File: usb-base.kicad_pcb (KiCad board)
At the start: 4 copper layers, 100 x 100 mm, 13 parts, among them J1 USB3_B, U1 CYUSB3082-FCAXI, U2 TPS25221, U3 TPS62161DSG, U4 LFE5U-25F-6BG256C, U6 TPS62162DSG

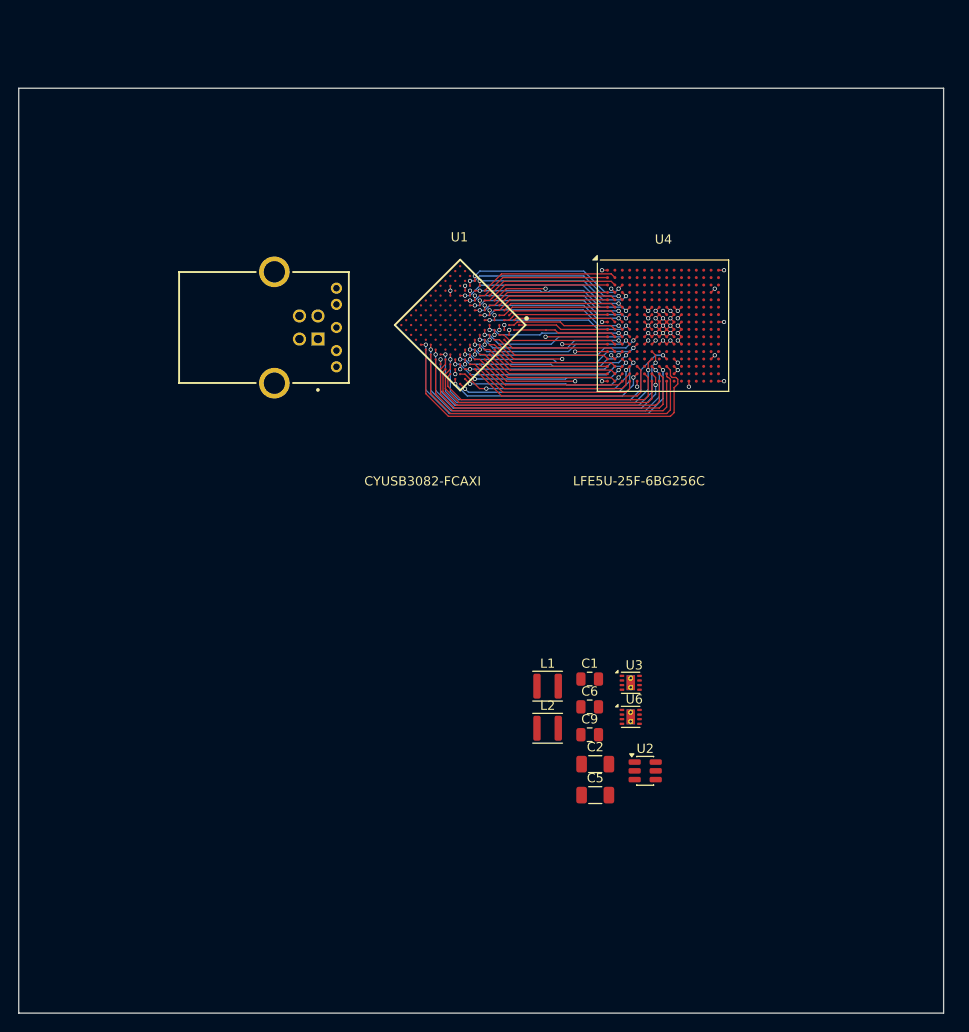
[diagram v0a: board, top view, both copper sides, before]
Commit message: Power supplies, oscillators, user IO breakout
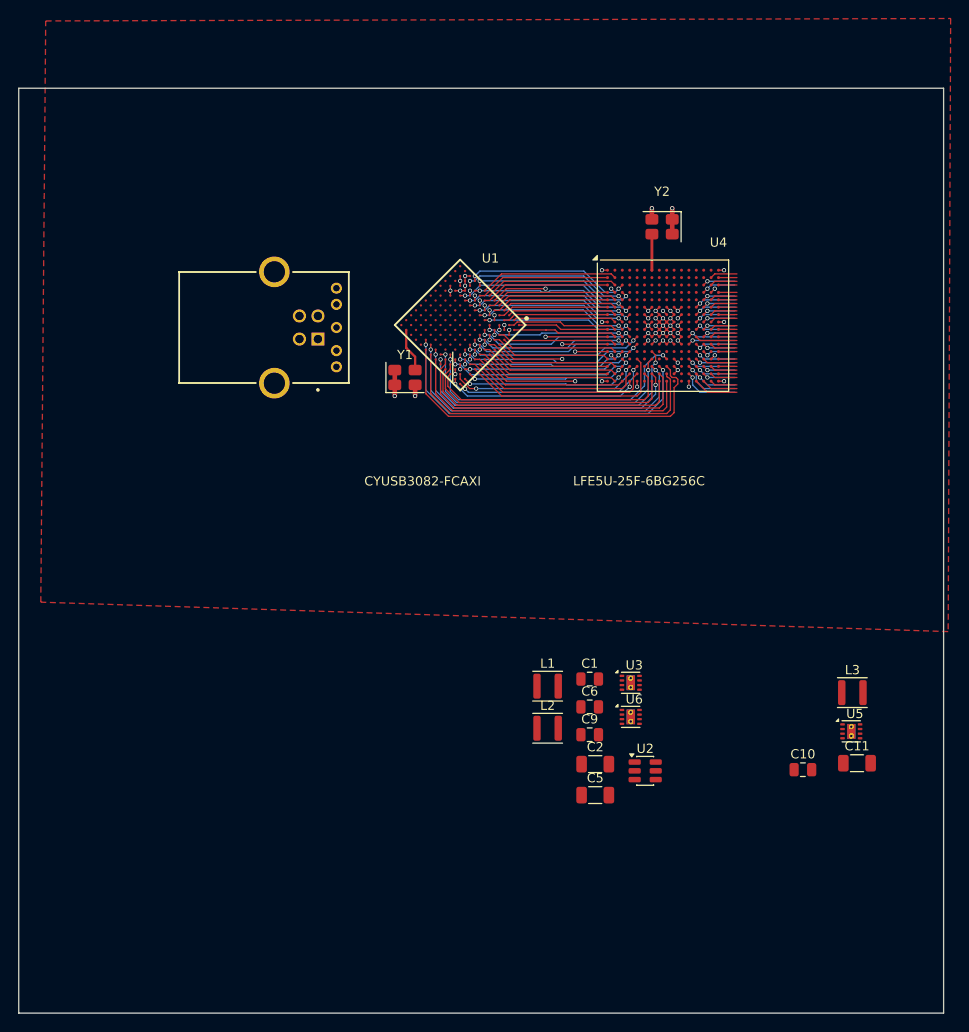
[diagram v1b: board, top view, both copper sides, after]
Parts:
- added C10: 10u, Capacitor_SMD:C_0805_2012Metric, F.Cu at (159.8, 107.2)
- added C11: 22u, Capacitor_SMD:C_1206_3216Metric, F.Cu at (165.7, 106.5)
- added L3: 2.2u, Inductor_SMD:L_Sunlord_SWPA3015S, F.Cu at (165.2, 98.9)
- added U5: TPS62160DSG, Package_SON:WSON-8-1EP_2x2mm_P0.5mm_EP0.9x1.6mm_ThermalVias, F.Cu at (165.1, 103.1)
- added Y1: 24MHz, Crystal:Crystal_SMD_SeikoEpson_TSX3225-4Pin_3.2x2.5mm, F.Cu at (116.8, 64.8)
- added Y2: 25MHz, Crystal:Crystal_SMD_SeikoEpson_TSX3225-4Pin_3.2x2.5mm, F.Cu at (144.6, 48.5)
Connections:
- U1 pad C11: +1V8 -> +3V3
- U1 pad F11: unconnected-(U1C-P13_0_PMODE-PadF11) -> PMODE
- U1 pad J12: unconnected-(U1C-P9_7_I2S0-RXMCLK-PadJ12) -> GPIO_1
- U1 pad J13: GPIO_1 -> unconnected-(U1C-P1_1_CC2-PadJ13)
- U1 pad M12: +1V8 -> +3V3
- U1 pad M13: unconnected-(U1C-P5_1_XTALOUT-PadM13) -> 24MHz
- U4 pad A7: unconnected-(U4B-PT38A/+/PCLKT0_0-PadA7) -> 25MHz
- U4 pad B15: unconnected-(U4D-PR11B/-/URC_GPLL0C_IN/HS/RDQ17-PadB15) -> D0_1
- U4 pad B16: unconnected-(U4D-PR11A/+/URC_GPLL0T_IN/HS/RDQ17-PadB16) -> D0_0
- U4 pad C14: unconnected-(U4D-PR11C/+/RDQ17-PadC14) -> D0_2
- U4 pad C15: unconnected-(U4D-PR14B/-/HS/RDQ17-PadC15) -> D0_5
- U4 pad C16: unconnected-(U4D-PR14A/+/HS/RDQ17-PadC16) -> D0_4
- U4 pad D14: unconnected-(U4D-PR11D/-/RDQ17-PadD14) -> D0_3
- U4 pad D16: unconnected-(U4D-PR17A/+/HS/RDQS17-PadD16) -> D0_8
- U4 pad E14: unconnected-(U4D-PR14C/+/RDQ17-PadE14) -> D0_6
- U4 pad E15: unconnected-(U4D-PR17B/-/HS/RDQSN17-PadE15) -> D0_9
- U4 pad E16: unconnected-(U4D-PR20D/-/RDQ17-PadE16) -> D0_13
- U4 pad F13: unconnected-(U4D-PR17C/+/RDQ17-PadF13) -> D0_10
- U4 pad F14: unconnected-(U4D-PR14D/-/RDQ17-PadF14) -> D0_7
- U4 pad F15: unconnected-(U4D-PR20C/+/RDQ17-PadF15) -> D0_12
- U4 pad F16: unconnected-(U4D-PR23A/+/HS/RDQ29-PadF16) -> D0_14
- U4 pad G13: unconnected-(U4D-PR20B/-/HS/RDQ17-PadG13) -> D0_11
- U4 pad G14: unconnected-(U4D-PR23C/+/VREF1_2/RDQ29-PadG14) -> D0_16
- U4 pad G15: unconnected-(U4D-PR23B/-/HS/RDQ29-PadG15) -> D0_15
- U4 pad G16: unconnected-(U4D-PR29A/+/GR_PCLK2_1/HS/RDQS29-PadG16) -> D0_20
- U4 pad H13: unconnected-(U4D-PR26B/-/HS/RDQ29-PadH13) -> D0_18
- U4 pad H14: unconnected-(U4D-PR23D/-/RDQ29-PadH14) -> D0_17
- U4 pad H15: unconnected-(U4D-PR29B/-/HS/RDQSN29-PadH15) -> D0_21
- U4 pad J13: unconnected-(U4D-PR26C/+/RDQ29-PadJ13) -> D0_19
- U4 pad J14: unconnected-(U4D-PR29C/+/GR_PCLK2_0/RDQ29-PadJ14) -> D0_22
- U4 pad J15: unconnected-(U4D-PR32B/-/PCLKC2_1/HS/RDQ29-PadJ15) -> D0_25
- U4 pad J16: unconnected-(U4D-PR32A/+/PCLKT2_1/HS/RDQ29-PadJ16) -> D0_24
- U4 pad K12: unconnected-(U4E-PR38B/-/HS/RDQ41-PadK12) -> D1_5
- U4 pad K13: unconnected-(U4E-PR38A/+/GR_PCLK3_0/HS/RDQ41-PadK13) -> D1_4
- U4 pad K14: unconnected-(U4D-PR29D/-/RDQ29-PadK14) -> D0_23
- U4 pad K15: unconnected-(U4D-PR32D/-/PCLKC2_0/RDQ29-PadK15) -> D0_27
- U4 pad K16: unconnected-(U4D-PR32C/+/PCLKT2_0/RDQ29-PadK16) -> D0_26
- U4 pad L12: unconnected-(U4E-PR38D/-/RDQ41-PadL12) -> D1_7
- U4 pad L13: unconnected-(U4E-PR38C/+/GR_PCLK3_1/RDQ41-PadL13) -> D1_6
- U4 pad L14: unconnected-(U4E-PR41C/+/RDQ41-PadL14) -> D1_10
- U4 pad L15: unconnected-(U4E-PR35B/-/PCLKC3_1/HS/RDQ41-PadL15) -> D1_1
- U4 pad L16: unconnected-(U4E-PR35A/+/PCLKT3_1/HS/RDQ41-PadL16) -> D1_0
- U4 pad M12: unconnected-(U4E-PR65C/+/RDQ65-PadM12) -> D1_25
- U4 pad M13: unconnected-(U4E-PR44C/+/RDQ41-PadM13) -> D1_14
- U4 pad M14: unconnected-(U4E-PR41D/-/RDQ41-PadM14) -> D1_11
- U4 pad M15: unconnected-(U4E-PR35D/-/PCLKC3_0/RDQ41-PadM15) -> D1_3
- U4 pad M16: unconnected-(U4E-PR35C/+/PCLKT3_0/RDQ41-PadM16) -> D1_2
- U4 pad N12: unconnected-(U4E-PR65D/-/RDQ65-PadN12) -> D1_26
- U4 pad N13: unconnected-(U4E-PR59A/+/HS/RDQ65-PadN13) -> D1_16
- U4 pad N14: unconnected-(U4E-PR44D/-/RDQ41-PadN14) -> D1_15
- U4 pad N16: unconnected-(U4E-PR41A/+/HS/RDQS41-PadN16) -> D1_8
- U4 pad N4: P1CTL8 -> unconnected-(U4F-PL59A/+/HS/LDQ65-PadN4)
- U4 pad N5: unconnected-(U4F-PL65D/-/LDQ65-PadN5) -> P1D13
- U4 pad P12: unconnected-(U4E-PR68D/-/LRC_GPLL0C_IN/RDQ65-PadP12) -> D1_27
- U4 pad P13: unconnected-(U4E-PR62A/+/HS/RDQ65-PadP13) -> D1_20
- U4 pad P14: unconnected-(U4E-PR59B/-/HS/RDQ65-PadP14) -> D1_17
- U4 pad P15: unconnected-(U4E-PR41B/-/HS/RDQSN41-PadP15) -> D1_9
- U4 pad P16: unconnected-(U4E-PR44A/+/HS/RDQ41-PadP16) -> D1_12
- U4 pad P5: P1D13 -> P1CTL8
- U4 pad R12: unconnected-(U4E-PR65A/+/HS/RDQS65-PadR12) -> D1_24
- U4 pad R13: unconnected-(U4E-PR62C/+/RDQ65-PadR13) -> D1_22
- U4 pad R14: unconnected-(U4E-PR62B/-/HS/RDQ65-PadR14) -> D1_21
- U4 pad R15: unconnected-(U4E-PR59C/+/RDQ65-PadR15) -> D1_18
- U4 pad R16: unconnected-(U4E-PR44B/-/VREF1_3/HS/RDQ41-PadR16) -> D1_13
- U4 pad R5: P1CTL9 -> P1D5
- U4 pad T14: unconnected-(U4E-PR62D/-/RDQ65-PadT14) -> D1_23
- U4 pad T15: unconnected-(U4E-PR59D/-/RDQ65-PadT15) -> D1_19
- U4 pad T4: P1D5 -> P1CTL9
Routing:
- net D1_27: track 0.00 -> 6.46 mm, vias 0 -> 1
- net D1_24: track 0.00 -> 6.30 mm, vias 0 -> 1
- net +3.3V: track 0.00 -> 5.60 mm, vias 0 -> 2
- net D1_26: track 0.00 -> 5.33 mm, vias 0 -> 1
- net D1_5: track 0.00 -> 5.33 mm, vias 0 -> 1
- net D1_7: track 0.00 -> 5.17 mm, vias 0 -> 1
- net GND: track 33.3 -> 38.3 mm, vias 35 -> 39
- net unconnected-(U4E-PR65B/-/HS/RDQSN65-PadT13): track 0.00 -> 4.90 mm
- net 24MHz: track 0.00 -> 4.74 mm
- net D1_22: track 0.00 -> 4.70 mm, vias 0 -> 1
- net D1_4: track 0.00 -> 4.57 mm
- net D1_14: track 0.00 -> 4.53 mm, vias 0 -> 1
- net D1_20: track 0.00 -> 4.53 mm, vias 0 -> 1
- net D0_10: track 0.00 -> 4.53 mm, vias 0 -> 1
- net D1_6: track 0.00 -> 4.53 mm, vias 0 -> 1
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- added copper zone on F.Cu, net GND

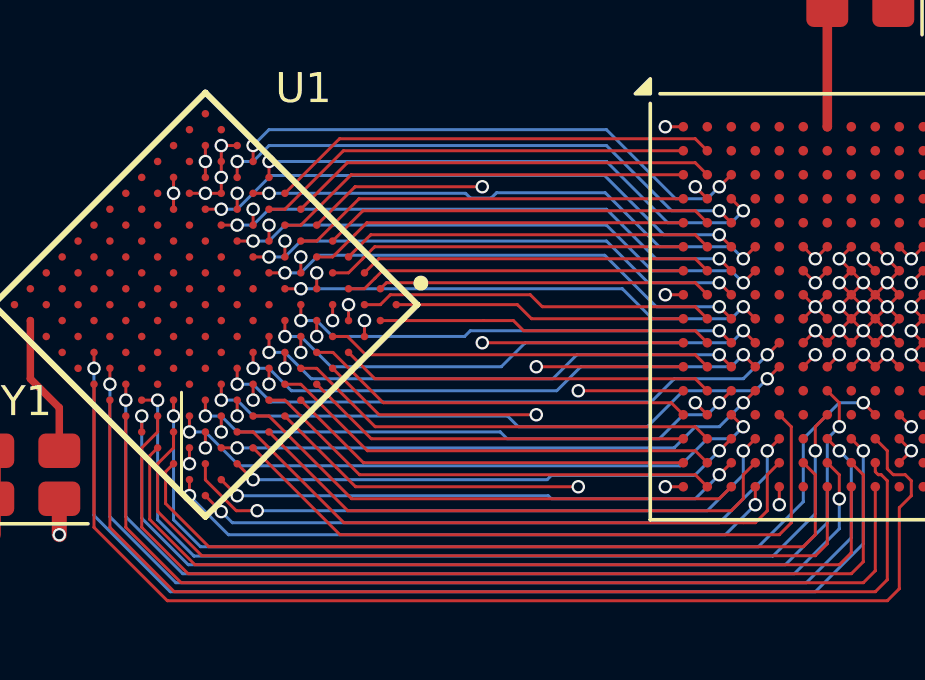
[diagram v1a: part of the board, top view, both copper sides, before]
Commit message: Remove DDR support in favour of cleaner bus routing
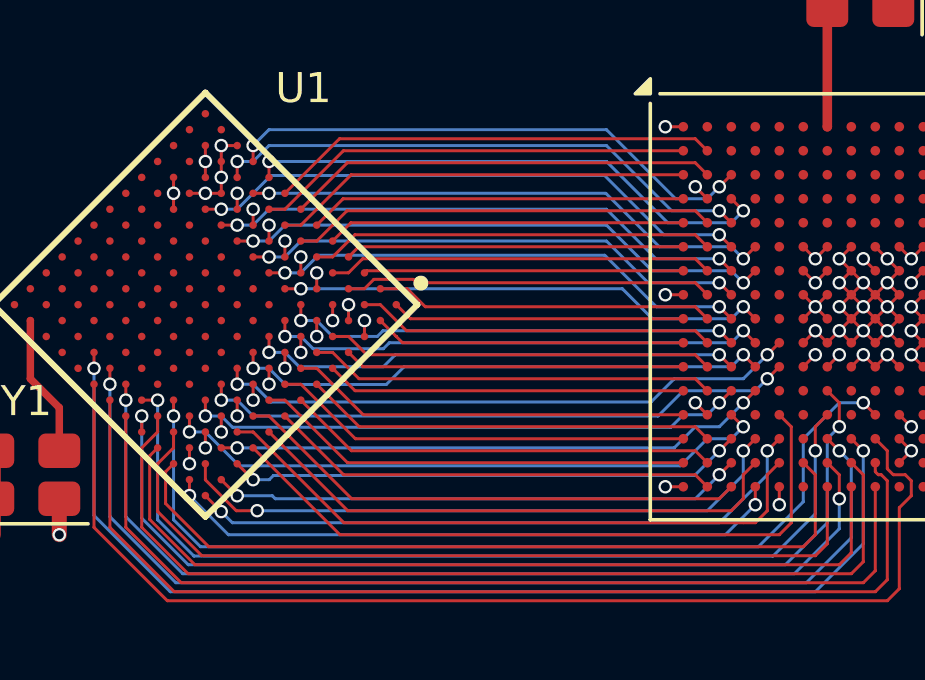
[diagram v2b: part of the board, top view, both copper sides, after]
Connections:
- U4 pad D1: P0CTL7 -> P0D9
- U4 pad E1: P0D4 -> P0D12
- U4 pad E2: P0D12 -> P0CTL7
- U4 pad F1: P0D5 -> P0D13
- U4 pad F2: P0D13 -> P0D4
- U4 pad G1: P0D6 -> P0D14
- U4 pad G2: P0D14 -> P0D5
- U4 pad H2: P0D15 -> P0D6
- U4 pad J2: P0D7 -> P0D15
- U4 pad K1: P0D9 -> P0CTL9
- U4 pad K2: P0CTL9 -> P0D7
- U4 pad L1: P1CLK -> P1D8
- U4 pad M1: P1D9 -> P1CLK
- U4 pad M2: P1D8 -> P1D1
- U4 pad N1: P1D1 -> P1D2
- U4 pad P1: P1D10 -> P1D3
- U4 pad P2: P1D2 -> P1D10
- U4 pad R1: P1D11 -> P1CTL7
- U4 pad R2: P1D3 -> P1D11
- U4 pad T2: P1CTL7 -> P1D9
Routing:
- net P0D9: track 17.9 -> 12.6 mm, vias 2 -> 0
- net P1D9: track 17.5 -> 15.1 mm, vias 2 -> 0
- net P1CLK: track 13.9 -> 12.0 mm, vias 2 -> 0
- net P0D13: track 12.4 -> 11.3 mm
- net P1D3: track 15.2 -> 14.0 mm
- net P1D2: track 14.5 -> 13.4 mm
- net P1CTL7: track 15.8 -> 14.7 mm
- net P0D14: track 11.8 -> 10.7 mm
- net P0D12: track 13.1 -> 11.9 mm
- net P1D8: track 12.5 -> 11.4 mm
- net P0D6: track 11.4 -> 12.3 mm
- net P0D4: track 12.7 -> 13.5 mm
- net P0D5: track 12.0 -> 12.8 mm
- net P0CTL7: track 13.3 -> 14.1 mm
- net P1D10: track 13.0 -> 13.8 mm
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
